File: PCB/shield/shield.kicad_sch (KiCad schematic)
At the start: 17 parts, among them J1 QTR-8A, J13 Motor, J3 Servo, J4 Battery, Q1 SI2301DS, SW1 SW_SPST, U1 WeAct-ESP32-S3-A, U3 TB6612FNG, U4 MP1584EN

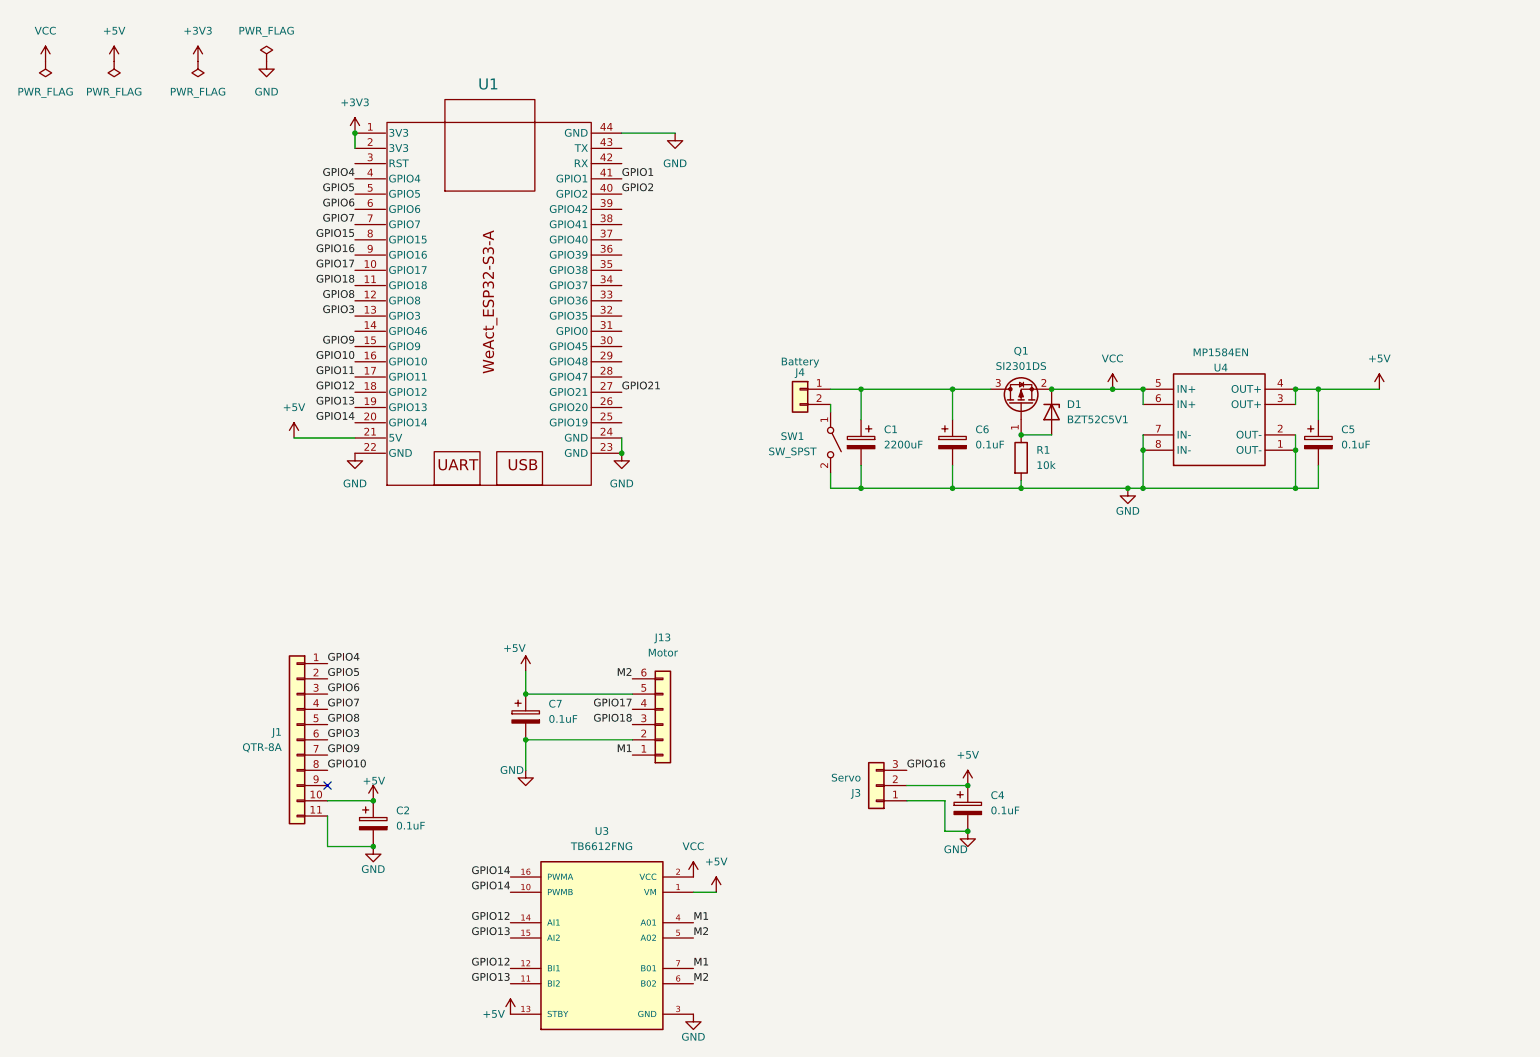
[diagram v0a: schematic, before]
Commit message: feat: rearrange pcb footprints; change mosfet
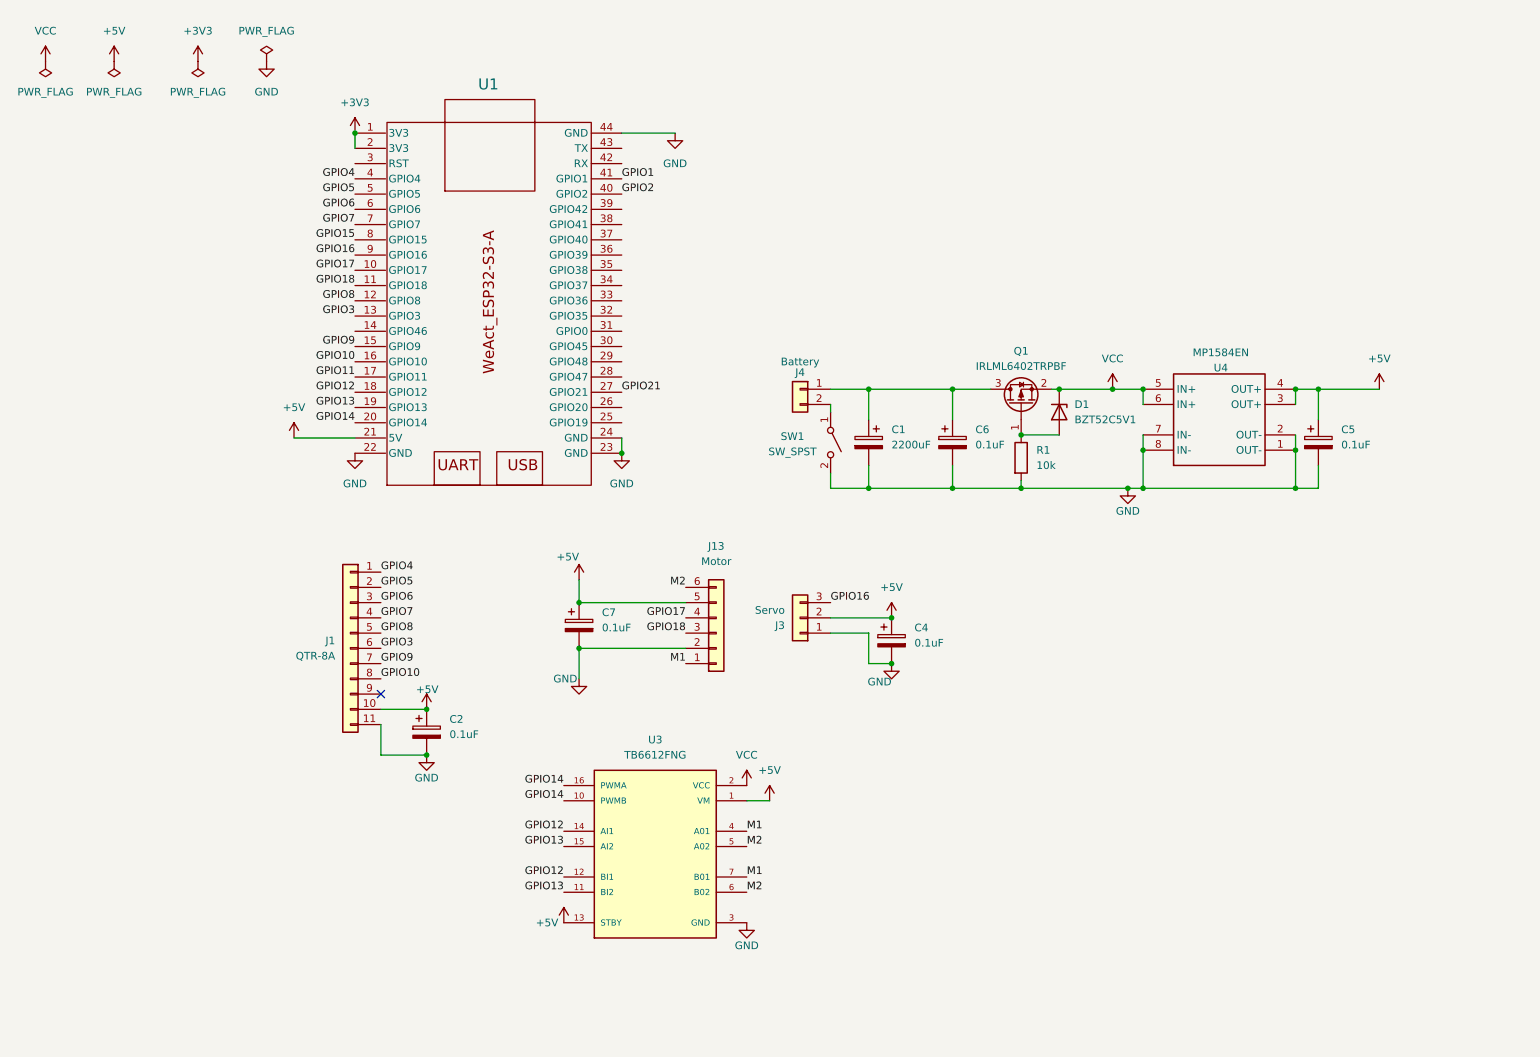
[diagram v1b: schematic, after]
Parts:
- Q1: value SI2301DS -> IRLML6402TRPBF
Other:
- moved on the sheet: C1, C2, C4, C7, D1, J1, J13, J3, U3

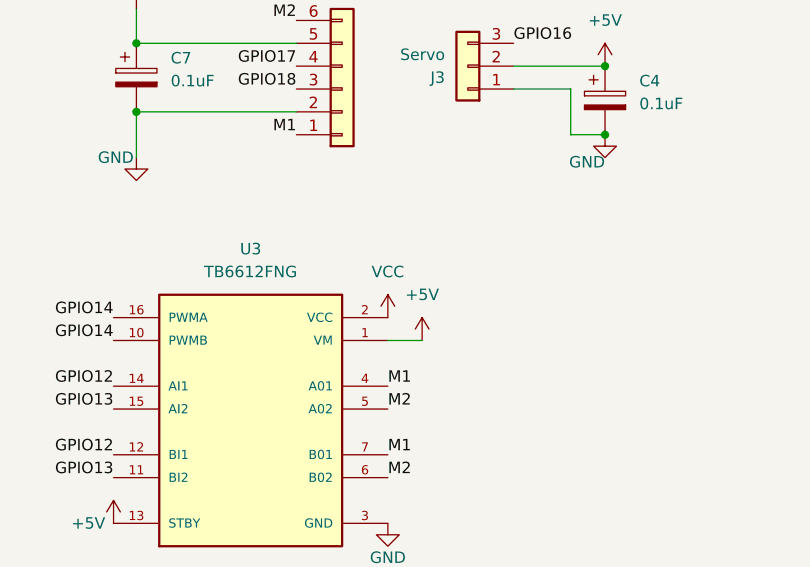
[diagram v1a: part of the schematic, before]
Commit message: fix: fix tb6612fng power input
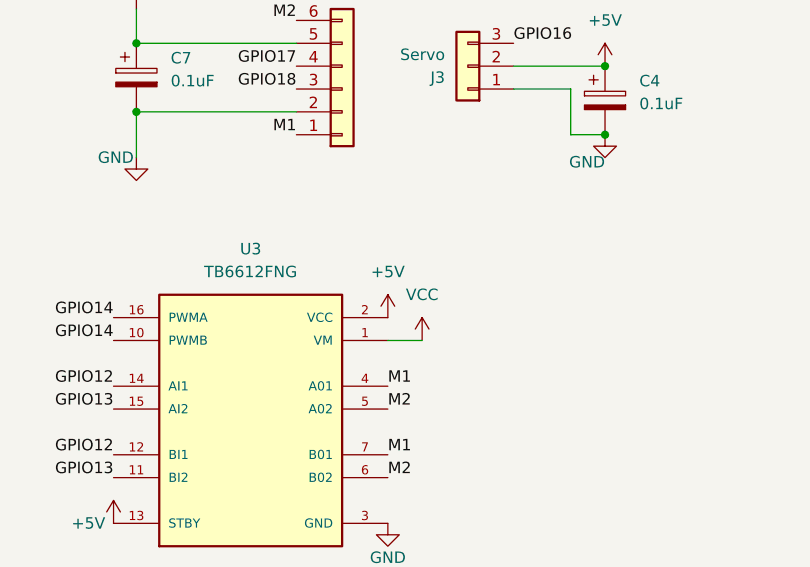
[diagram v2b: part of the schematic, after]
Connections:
- net +5V: now also U3.2 (VCC); no longer U3.1 (VM)
- net VCC: now also U3.1 (VM); no longer U3.2 (VCC)
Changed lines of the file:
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@@
 	(symbol
 		(lib_id "power:+5V")
-		(at 147.32 148.59 0)
+		(at 143.51 146.05 0)
 		(unit 1)
 		(exclude_from_sim no)
@@
 		(dnp no)
 		(property "Reference" "#PWR013"
-			(at 147.32 152.4 0)
+			(at 143.51 149.86 0)
 			(effects
 				(font
@@
 		)
 		(property "Value" "+5V"
-			(at 147.32 143.51 0)
-			(effects
-				(font
-					(size 1.27 1.27)
-				)
-			)
-		)
-		(property "Footprint" ""
-			(at 147.32 148.59 0)
+			(at 143.51 140.97 0)
+			(effects
+				(font
+					(size 1.27 1.27)
+				)
+			)
+		)
+		(property "Footprint" ""
+			(at 143.51 146.05 0)
 			(effects
 				(font
@@
 		)
 		(property "Datasheet" ""
-			(at 147.32 148.59 0)
+			(at 143.51 146.05 0)
 			(effects
 				(font
@@
 		)
 		(property "Description" "Power symbol creates a global label with name \"+5V\""
-			(at 147.32 148.59 0)
+			(at 143.51 146.05 0)
 			(effects
 				(font
@@
 	(symbol
 		(lib_id "power:VCC")
-		(at 143.51 146.05 0)
+		(at 147.32 148.59 0)
 		(unit 1)
 		(exclude_from_sim no)
@@
 		(fields_autoplaced yes)
 		(property "Reference" "#PWR05"
-			(at 143.51 149.86 0)
+			(at 147.32 152.4 0)
 			(effects
 				(font
@@
 		)
 		(property "Value" "VCC"
-			(at 143.51 140.97 0)
-			(effects
-				(font
-					(size 1.27 1.27)
-				)
-			)
-		)
-		(property "Footprint" ""
-			(at 143.51 146.05 0)
+			(at 147.32 143.51 0)
+			(effects
+				(font
+					(size 1.27 1.27)
+				)
+			)
+		)
+		(property "Footprint" ""
+			(at 147.32 148.59 0)
 			(effects
 				(font
@@
 		)
 		(property "Datasheet" ""
-			(at 143.51 146.05 0)
+			(at 147.32 148.59 0)
 			(effects
 				(font
@@
 		)
 		(property "Description" "Power symbol creates a global label with name \"VCC\""
-			(at 143.51 146.05 0)
-			(effects
-				(font
+			(at 147.32 148.59 0)
+			(effects
+				(font

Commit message: feat: fix some bugs and add some features in pcb design
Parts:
- added C10, C11, C8, C9: 0.1uF, Capacitor_SMD:C_0805_2012Metric_Pad1.18x1.45mm_HandSolder, symbol Device:C_Polarized
- added C3: 10uF, Capacitor_SMD:CP_Elec_4x5.4, symbol Device:C_Polarized
- added D2: SS34, Diode_SMD:D_SMA, symbol Diode:SS34
- added D3: SMAJ5.0A, Diode_SMD:D_SMB_Handsoldering, symbol Device:D_TVS
- added D4: SMBJ12CA, Diode_SMD:D_SMB_Handsoldering, symbol Device:D_TVS
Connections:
- net +5V: now also C11.1, C8.1, D2.1 (K); no longer C5.1, U4.3 (OUT+), U4.4 (OUT+)
- net GND: now also C10.2, C11.2, C3.2, C8.2, C9.2, D3.1 (A1), D4.1 (A1)
- net at J4.1 (Pin_1), Q1.3 (D): no longer C1.1, C6.1
- net VCC renamed +12V
- net +12V: now also C1.1, C6.1, C10.1, C3.1, C9.1, D4.2 (A2)
- new net: C5.1, D2.2 (A), D3.2 (A2), U4.3 (OUT+), U4.4 (OUT+)
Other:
- moved on the sheet: C1, C2, C4, C5, C6, C7, D1, J1, J13, J3, J4, Q1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
